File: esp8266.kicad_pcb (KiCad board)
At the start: 2 copper layers, 54.6 x 16.5 mm, 11 parts, among them U10 TS-1187A-B-A-B, U11 W25Q128JVSIQTR, U2 ESP8266EX, U3 AP2112K-3_3TRG1, U4 HDC1080DMBR, U5 MCP73831T-2ACI_OT, U6 MK-12C02-G020, U7 S2B-PH-SM4-TB(LF)(SN), U8 SK6812MINI-HS, U9 UMH3N

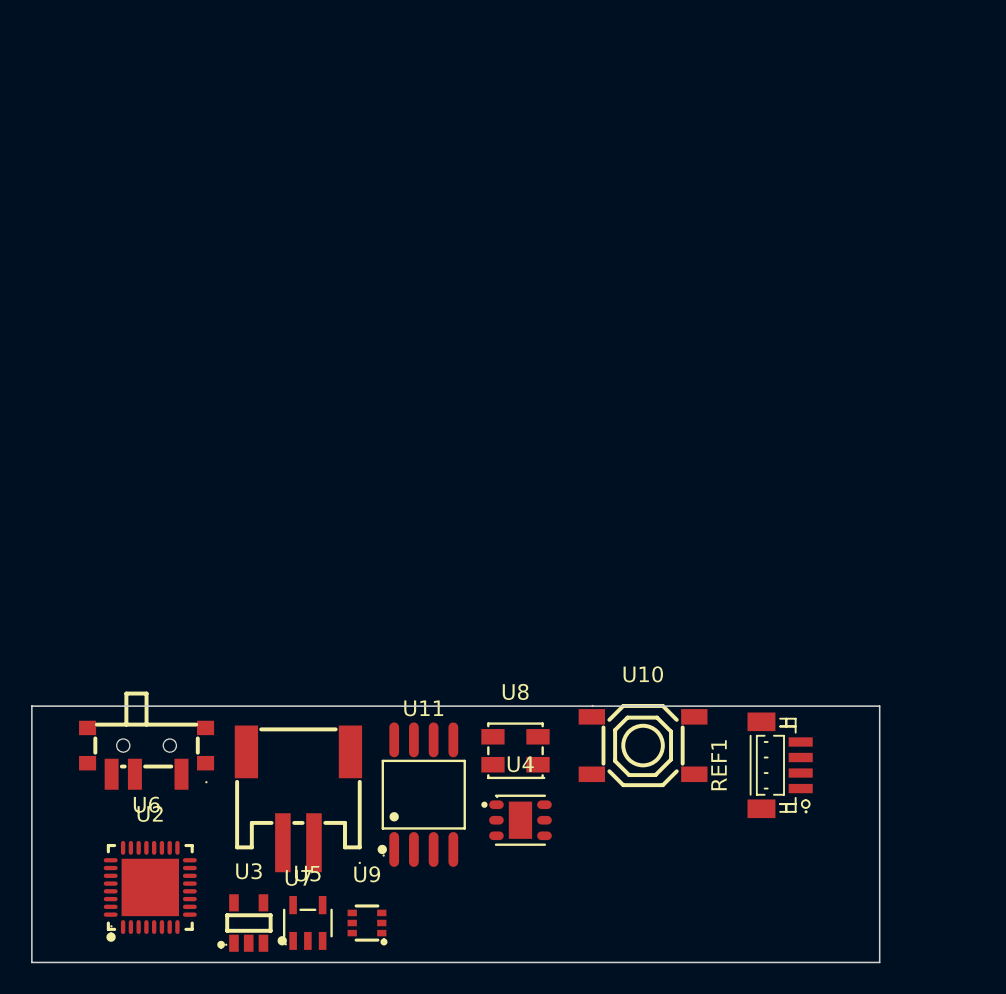
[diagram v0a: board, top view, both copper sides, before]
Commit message: Schematic done
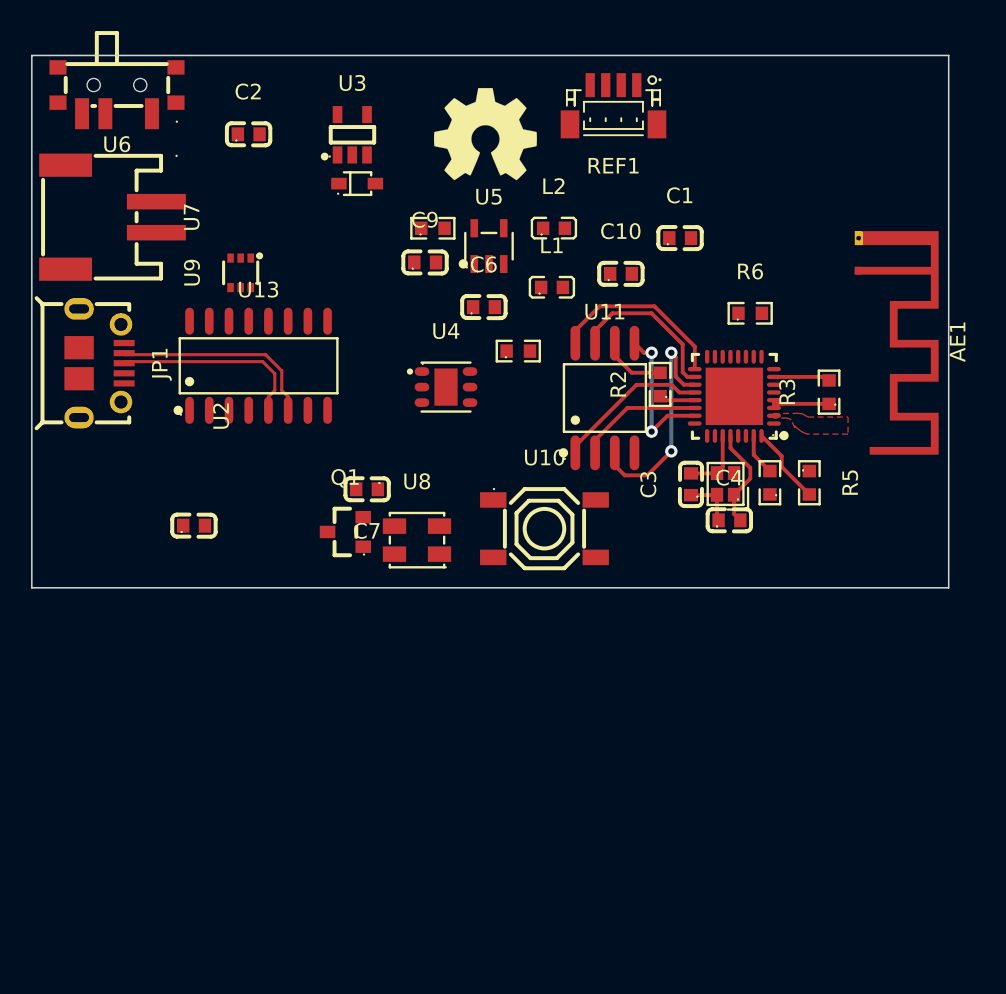
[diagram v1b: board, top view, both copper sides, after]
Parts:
- added AE1: Antenna_Shield, RF_Antenna:Texas_SWRA117D_2.4GHz_Right, F.Cu at (165.0, 49.4)
- added C1: 10u, jlc_footprints:C0603, F.Cu at (153.5, 47.3)
- added C10: 100n, jlc_footprints:C0603, F.Cu at (149.7, 49.6)
- added C2: 100n, jlc_footprints:C0603, F.Cu at (125.7, 40.6)
- added C3: 10p, jlc_footprints:C0603, F.Cu at (154.2, 63.2)
- added C4: 10p, jlc_footprints:C0603, F.Cu at (156.7, 65.5)
- added C5: 4.7u, jlc_footprints:C0603, F.Cu at (122.2, 65.8)
- added C6: 5.6p, jlc_footprints:C0603, F.Cu at (140.9, 51.8)
- added C7: 1u, jlc_footprints:C0603, F.Cu at (133.3, 63.5)
- added C9: 2.2u, jlc_footprints:C0603, F.Cu at (137.1, 48.9)
- added D3: BAT20JFILM, jlc_footprints:SOD-323_L1.8-W1.3-LS2.5-RD, F.Cu at (132.7, 43.8)
- added JP1: USB_B_Micro, jlc_footprints:MICRO-USB-SMD_1050171001, F.Cu at (116.3, 55.4)
- added L1: DNP, jlc_footprints:L0603, F.Cu at (145.3, 50.5)
- added L2: DNP, jlc_footprints:L0603, F.Cu at (145.4, 46.7)
- added OSHW1: github.com/besi/stepomatic, Symbol:OSHW-Symbol_6.7x6mm_SilkScreen, F.Cu at (141.0, 40.6)
- added Q1: AO3401A, jlc_footprints:SOT-23_L2.9-W1.3-P1.90-LS2.4-BR, F.Cu at (132.0, 66.3)
- added R1: 12k, jlc_footprints:R0603, F.Cu at (159.3, 63.1)
- added R2: 200, jlc_footprints:R0603, F.Cu at (152.2, 56.8)
- added R3: 10k, jlc_footprints:R0603, F.Cu at (163.1, 57.2)
- added R4: 2k, jlc_footprints:R0603, F.Cu at (137.6, 46.7)
- added R5: 10k, jlc_footprints:R0603, F.Cu at (161.8, 63.1)
- added R6: 10k, jlc_footprints:R0603, F.Cu at (158.0, 52.2)
- added R7: 10k, jlc_footprints:R0603, F.Cu at (143.1, 54.6)
- added U13: CH340C, jlc_footprints:SOP-16_L10.0-W3.9-P1.27-LS6.0-BL, F.Cu at (126.4, 55.5)
- added Y1: 26Mhz, jlc_footprints:CRYSTAL-SMD_4P-L2.0-W1.6-BL, F.Cu at (156.4, 63.2)
- moved U3 51.2 mm to (132.4, 40.7)
- moved U2 49.2 mm to (157.0, 57.5), turned to 90 degrees
- moved U5 45.1 mm to (141.2, 47.8)
- moved REF1 43.9 mm to (149.2, 38.7), turned to 180 degrees
- moved U9 42.7 mm to (125.2, 49.6), turned to 90 degrees
- moved U6 42.6 mm to (117.2, 37.8)
- moved U7 39.3 mm to (116.9, 46.0), turned to -90 degrees
- moved U4 28.3 mm to (138.4, 56.9)
- moved U11 28.1 mm to (148.7, 57.6)
- moved U10 15.3 mm to (144.8, 66.0)
- moved U8 15.0 mm to (136.6, 66.8)
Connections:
- REF1 pad 0: unconnected-(REF1-Pad0) -> GND
- REF1 pad 1: unconnected-(REF1-Pad1) -> GND
- REF1 pad 2: unconnected-(REF1-Pad2) -> +3V3
- REF1 pad 3: unconnected-(REF1-Pad3) -> GPIO2
- REF1 pad 4: unconnected-(REF1-Pad4) -> GPIO14
- U11 pad 1: unconnected-(U11-CS#-Pad1) -> SD_CS0
- U11 pad 2: unconnected-(U11-DO-Pad2) -> SD_SO
- U11 pad 3: unconnected-(U11-IO2-Pad3) -> SD_WP
- U11 pad 4: unconnected-(U11-GND-Pad4) -> GND
- U11 pad 5: unconnected-(U11-DI-Pad5) -> SD_SI
- U11 pad 6: unconnected-(U11-CLK-Pad6) -> SD_CLK
- U11 pad 7: unconnected-(U11-IO3-Pad7) -> SD_HD
- U11 pad 8: unconnected-(U11-VCC-Pad8) -> +3V3
- U2 pad 1: unconnected-(U2-VDDA-Pad1) -> +3V3
- U2 pad 10: unconnected-(U2-MTDI-Pad10) -> GPIO12
- U2 pad 11: unconnected-(U2-VDDPST-Pad11) -> +3V3
- U2 pad 12: unconnected-(U2-MTCK-Pad12) -> GPIO13
- U2 pad 13: unconnected-(U2-MTDO-Pad13) -> GPIO15
- U2 pad 14: unconnected-(U2-GPIO2-Pad14) -> GPIO2
- U2 pad 15: unconnected-(U2-GPIO0-Pad15) -> GPIO0
- U2 pad 16: unconnected-(U2-GPIO4-Pad16) -> GPIO4
- U2 pad 17: unconnected-(U2-VDDPST-Pad17) -> +3V3
- U2 pad 18: unconnected-(U2-SDIO_DATA_2-Pad18) -> SD_HD
- U2 pad 19: unconnected-(U2-SDIO_DATA_3-Pad19) -> SD_WP
- U2 pad 2: unconnected-(U2-LNA-Pad2) -> LNA
- U2 pad 20: unconnected-(U2-SDIO_CMD-Pad20) -> SD_CS0
- U2 pad 21: unconnected-(U2-SDIO_CLK-Pad21) -> Net-(U2-SDIO_CLK)
- U2 pad 22: unconnected-(U2-SDIO_DATA_0-Pad22) -> SD_SO
- U2 pad 23: unconnected-(U2-SDIO_DATA_1-Pad23) -> SD_SI
- U2 pad 24: unconnected-(U2-GPIO5-Pad24) -> GPIO5
- U2 pad 25: unconnected-(U2-U0RXD-Pad25) -> U0RXD
- U2 pad 26: unconnected-(U2-U0TXD-Pad26) -> U0TXD
- U2 pad 27: unconnected-(U2-XTAL_OUT-Pad27) -> Net-(U2-XTAL_OUT)
- U2 pad 28: unconnected-(U2-XTAL_IN-Pad28) -> Net-(U2-XTAL_IN)
- U2 pad 29: unconnected-(U2-VDDD-Pad29) -> +3V3
- U2 pad 3: unconnected-(U2-VDD3P3-Pad3) -> +3V3
- U2 pad 30: unconnected-(U2-VDDA-Pad30) -> +3V3
- U2 pad 31: unconnected-(U2-RES12K-Pad31) -> Net-(U2-RES12K)
- U2 pad 32: unconnected-(U2-~{EXT_RSTB}-Pad32) -> RESET
- U2 pad 33: unconnected-(U2-GND-Pad33) -> GND
- U2 pad 4: unconnected-(U2-VDD3P3-Pad4) -> +3V3
- U2 pad 6: unconnected-(U2-TOUT-Pad6) -> ADC
- U2 pad 7: unconnected-(U2-CHIP_PU-Pad7) -> Net-(U2-CHIP_PU)
- U2 pad 8: unconnected-(U2-XPD_DCDC-Pad8) -> GPIO16
- U2 pad 9: unconnected-(U2-MTMS-Pad9) -> GPIO14
- U3 pad 1: unconnected-(U3-VIN-Pad1) -> Net-(D3-K)
- U3 pad 2: unconnected-(U3-GND-Pad2) -> GND
- U3 pad 3: unconnected-(U3-EN-Pad3) -> Net-(U3-EN)
- U3 pad 5: unconnected-(U3-VOUT-Pad5) -> +3V3
- U4 pad 1: unconnected-(U4-SDA-Pad1) -> GPIO2
- U4 pad 2: unconnected-(U4-GND-Pad2) -> GND
- U4 pad 5: unconnected-(U4-VDD-Pad5) -> +3V3
- U4 pad 6: unconnected-(U4-SCL-Pad6) -> GPIO14
- U4 pad 7: unconnected-(U4-EP-Pad7) -> GND
- U5 pad 2: unconnected-(U5-VSS-Pad2) -> GND
- U5 pad 3: unconnected-(U5-VBAT-Pad3) -> +BATT
- U5 pad 4: unconnected-(U5-VDD-Pad4) -> VBUS
- U5 pad 5: unconnected-(U5-PROG-Pad5) -> Net-(U5-PROG)
- U6 pad 1: unconnected-(U6-Pad1) -> Net-(D3-K)
- U6 pad 2: unconnected-(U6-Pad2) -> Net-(U3-EN)
- U6 pad 3: unconnected-(U6-Pad3) -> GND
- U7 pad 1: unconnected-(U7-Pad1) -> GND
- U7 pad 2: unconnected-(U7-Pad2) -> +BATT
- U8 pad 1: unconnected-(U8-GND-Pad1) -> GND
- U8 pad 2: unconnected-(U8-DIN-Pad2) -> NEOPIXEL
- U8 pad 3: unconnected-(U8-VDD-Pad3) -> +3V3
- U8 pad 4: unconnected-(U8-DOUT-Pad4) -> NEOPIXEL_OUT
- U9 pad 1: unconnected-(U9-E-Pad1) -> DTR
- U9 pad 2: unconnected-(U9-B-Pad2) -> RTS
- U9 pad 3: unconnected-(U9-C-Pad3) -> RESET
- U9 pad 4: unconnected-(U9-E-Pad4) -> RTS
- U9 pad 5: unconnected-(U9-B-Pad5) -> DTR
- U9 pad 6: unconnected-(U9-C-Pad6) -> GPIO0
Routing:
- net +3V3: track 0.00 -> 15.8 mm
- net SD_WP: track 0.00 -> 14.8 mm, vias 0 -> 2
- net /UD_N: track 0.00 -> 13.4 mm
- net /UD_P: track 0.00 -> 12.6 mm
- net SD_HD: track 0.00 -> 10.4 mm
- net SD_CS0: track 0.00 -> 9.97 mm
- net SD_SI: track 0.00 -> 9.64 mm, vias 0 -> 2
- net SD_SO: track 0.00 -> 8.09 mm
- net Net-(U2-XTAL_IN): track 0.00 -> 6.56 mm
- net RESET: track 0.00 -> 5.04 mm
- net Net-(U2-XTAL_OUT): track 0.00 -> 4.23 mm
- net SD_CLK: track 0.00 -> 4.18 mm
- net Net-(U2-CHIP_PU): track 0.00 -> 3.65 mm
- net GND: track 0.00 -> 3.37 mm
- net Net-(U2-RES12K): track 0.00 -> 2.69 mm
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- added copper zone on F.Cu, net LNA
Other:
- board size 54.6 x 16.5 mm -> 59.1 x 34.3 mm

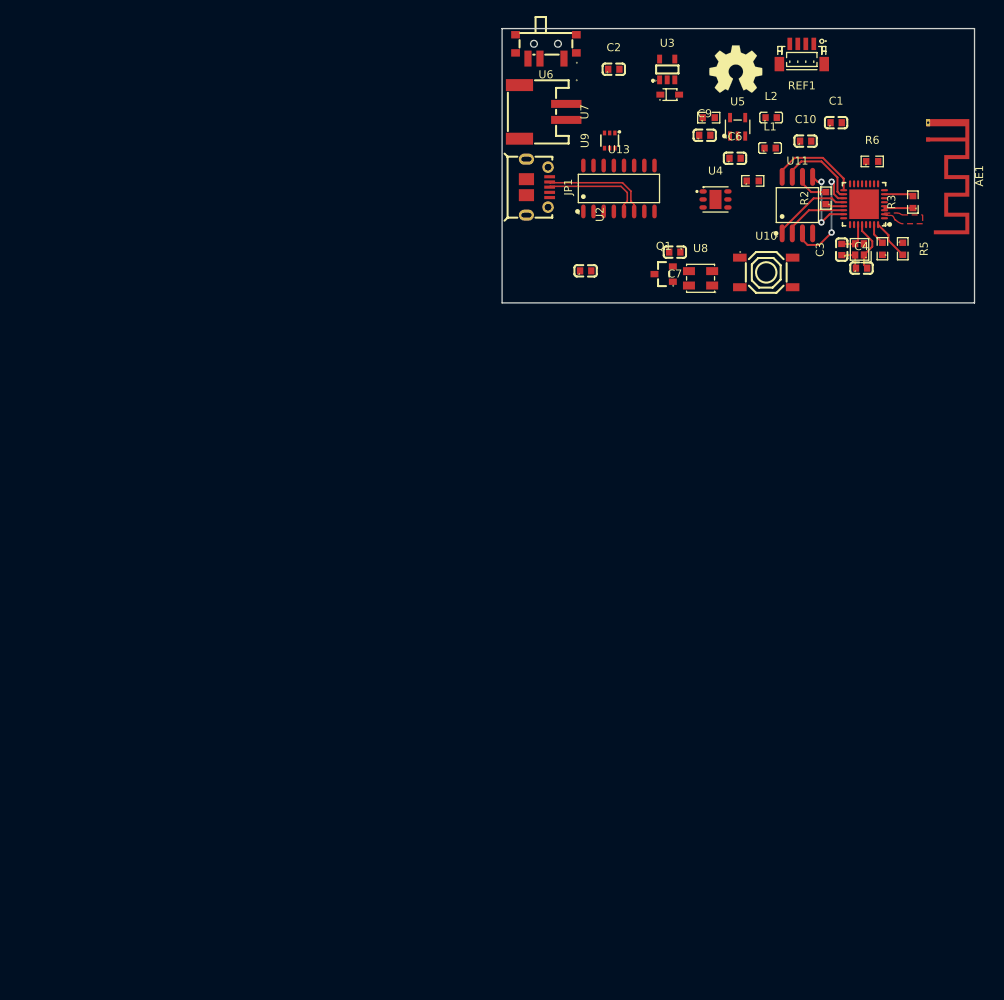
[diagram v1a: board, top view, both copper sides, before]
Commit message: Add antenna and layout the board
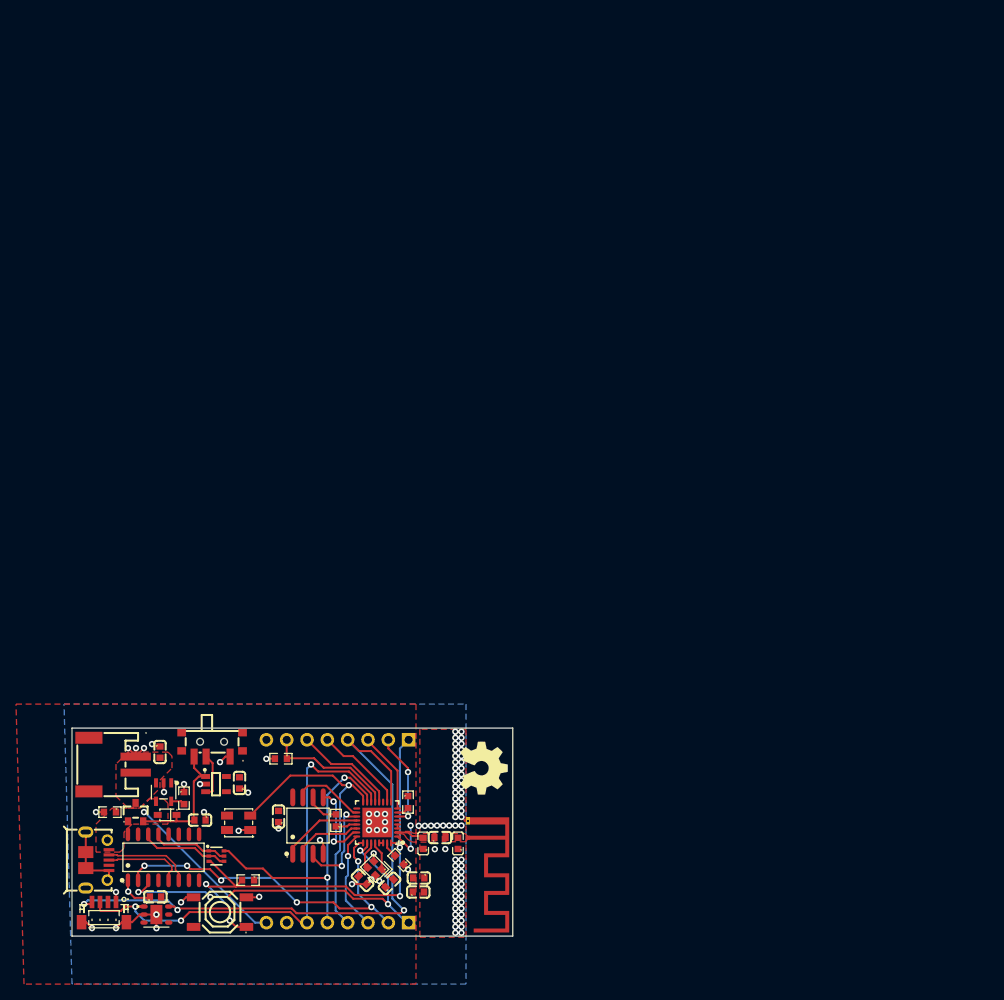
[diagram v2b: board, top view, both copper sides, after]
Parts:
- removed AE1: Antenna_Shield, RF_Antenna:Texas_SWRA117D_2.4GHz_Right
- added C8: 100n, jlc_footprints:C0603, F.Cu at (68.4, 144.1)
- added E2: Antenna_Trace, RF_Antenna:Texas_SWRA117D_2.4GHz_Right, F.Cu at (107.5, 136.7)
- added J1: Conn_01x08, Connector_PinHeader_2.54mm:PinHeader_1x08_P2.54mm_Vertical, B.Cu at (100.1, 124.5)
- added J2: Conn_01x08, Connector_PinHeader_2.54mm:PinHeader_1x08_P2.54mm_Vertical, B.Cu at (100.1, 147.3)
- moved REF1 138.3 mm to (62.0, 146.0)
- moved R5 113.7 mm to (80.0, 142.0), turned to 180 degrees
- moved U4 113.5 mm to (68.5, 146.3)
- moved R7 112.6 mm to (62.7, 133.5), turned to 180 degrees
- moved U5 109.8 mm to (69.4, 131.0), turned to 180 degrees
- moved D3 109.8 mm to (69.9, 133.9), turned to 180 degrees
- moved C1 109.4 mm to (101.3, 143.5)
- moved R4 107.4 mm to (72.0, 131.8), turned to -90 degrees
- moved C10 107.1 mm to (83.8, 134.1), turned to 90 degrees
- moved U3 105.6 mm to (76.0, 130.0), turned to -90 degrees
- moved U10 105.1 mm to (76.5, 146.0), turned to 180 degrees
- moved R6 105.1 mm to (84.1, 126.8), turned to 180 degrees
- moved C2 104.0 mm to (101.3, 141.7), turned to 180 degrees
- moved U9 102.1 mm to (76.1, 139.0), turned to 180 degrees
- moved U13 101.1 mm to (69.4, 139.2)
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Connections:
- net Net-(AE1-A) renamed ANT
- U10 pad 1: unconnected-(U10-A-Pad1) -> RESET
- U10 pad 3: unconnected-(U10-C-Pad3) -> GND
- U10 pad 4: unconnected-(U10-D-Pad4) -> GND
- U6 pad 1: Net-(D3-K) -> GND
- U6 pad 3: GND -> Net-(D3-K)
- U8 pad 2: NEOPIXEL -> GPIO4
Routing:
- net GPIO14: track 0.00 -> 78.7 mm, vias 0 -> 3
- net GPIO2: track 0.00 -> 61.5 mm, vias 0 -> 3
- net RESET: track 5.04 -> 60.2 mm, vias 0 -> 4
- net GND: track 3.37 -> 55.7 mm, vias 0 -> 102
- net U0TXD: track 0.00 -> 47.9 mm, vias 0 -> 4
- net U0RXD: track 0.00 -> 45.7 mm, vias 0 -> 6
- net GPIO0: track 0.00 -> 38.0 mm, vias 0 -> 2
- net GPIO4: track 0.00 -> 36.5 mm, vias 0 -> 1
- net VBUS: track 0.00 -> 21.0 mm, vias 0 -> 1
- net Net-(D3-K): track 0.00 -> 17.2 mm
- net GPIO15: track 0.00 -> 16.4 mm
- net GPIO13: track 0.00 -> 13.0 mm
- net GPIO5: track 0.00 -> 12.5 mm, vias 0 -> 1
- net ADC: track 0.00 -> 11.9 mm, vias 0 -> 2
- net GPIO12: track 0.00 -> 11.6 mm
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- added copper zone on F.Cu, net +3V3
- added copper zone on F.Cu, net +BATT
- added copper zone on F.Cu, net ANT
- added copper zone on B.Cu, net GND
- added copper zone on F.Cu, net GND
- added copper zone on F.Cu, net VBUS
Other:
- board size 59.1 x 34.3 mm -> 55.1 x 26 mm
